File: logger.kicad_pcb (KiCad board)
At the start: 4 copper layers, 50.8 x 25.4 mm, 82 parts, among them IC1 ATMEGA1284P-A, P1 CONN_5X2, P2 CONN_2, U1 LT1615-1, U10 SN74AUP1G00, U2 AT45DB321D, U3 MCP6054, U4 MAX11612, U5 TPS7703X, U6 ADXL337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

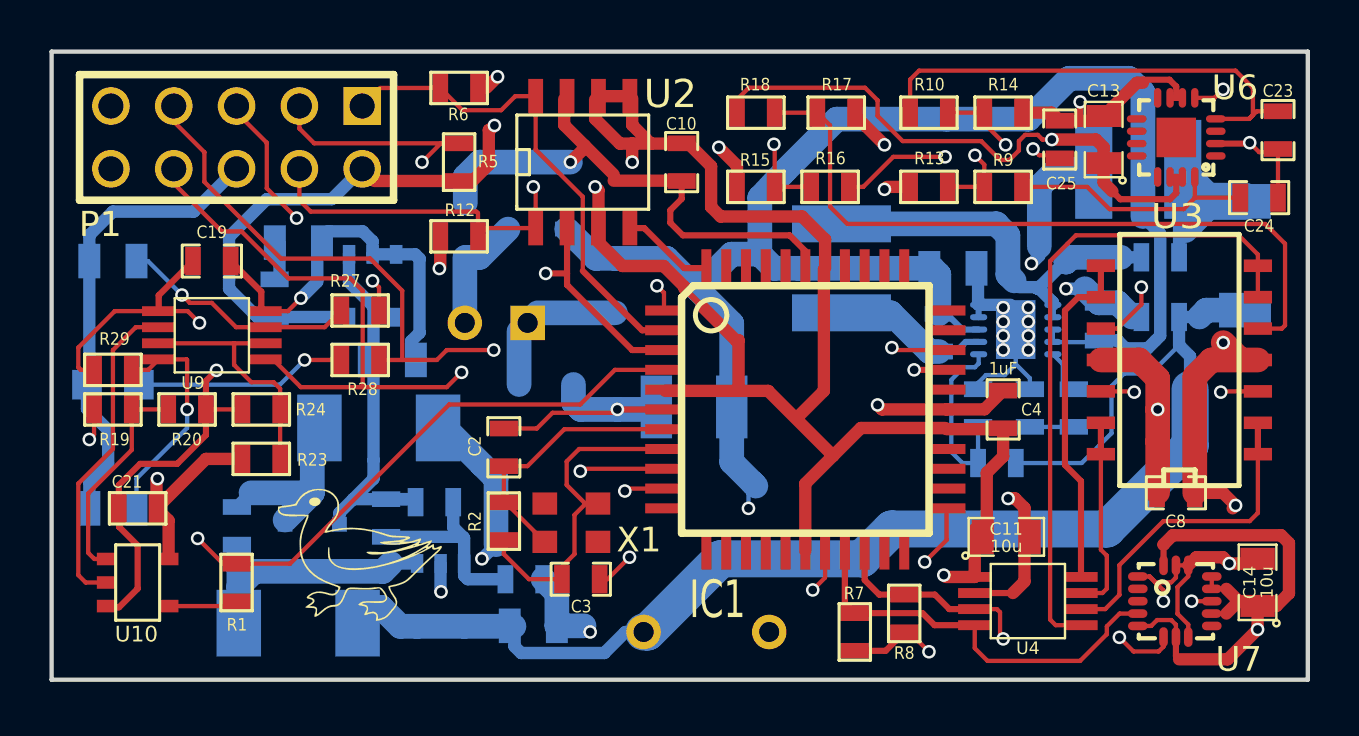
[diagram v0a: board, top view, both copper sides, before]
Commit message: General layout/grounding tweaks, DC-DC layout improved, ADC set up for Vdd as ref, switchable 3v3_Analog for lower standby power, reset circuitry redone, Footprint fixes, better silkscreen.
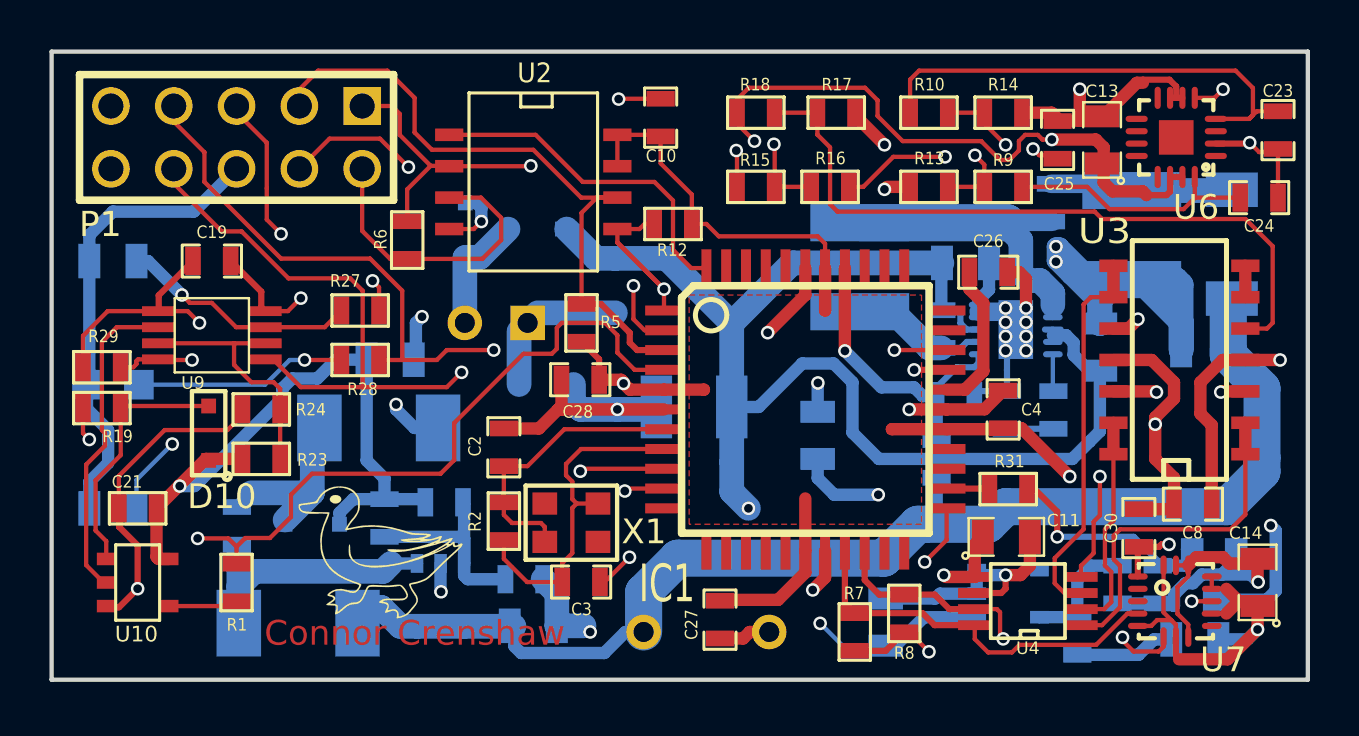
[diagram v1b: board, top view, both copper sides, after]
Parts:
- added C26: C, SM0603_Capa, F.Cu at (142.4, 100.5)
- added C27: 1u, SM0603_Capa, F.Cu at (131.6, 114.6)
- added C28: 1u, SM0603_Capa, F.Cu at (125.9, 104.9)
- added C29: 10u, SM0805, B.Cu at (138.2, 114.7)
- added C30: 1u, SM0603_Capa, F.Cu at (148.5, 110.9)
- added D10: DIODESCH, SOD323, F.Cu at (110.9, 107.1)
- added L5: 10u, SM0805, B.Cu at (135.5, 107.2)
- added Q1: MOS_P, SOT23GDS, B.Cu at (151.5, 112.8)
- added R30: 1, SM0603, B.Cu at (147.6, 113.2)
- added R31: 1k, SM0603, F.Cu at (143.2, 109.3)
- C18, C22: footprint SM0603_Capa -> SM0805
- C19: value .1 -> .1u
- D6: footprint DO128 -> SOD128
- R19: value 750k -> 100k
- R20: value 250k -> 1M; moved to B.Cu
- U2: value AT45DB321D -> SST25VF064C; footprint SO8E -> SST25_S3A
- U3: footprint SO14N -> SO14E
- U6: footprint LFCSP8 -> LFCSP16
- moved R20 39.9 mm to (149.3, 113.2), turned to 90 degrees
- moved C12 39.6 mm to (150.8, 115.4)
- moved R11 35.2 mm to (146.0, 115.3), turned to 270 degrees
- moved U5 28.6 mm to (143.2, 113.5), turned to 90 degrees
- moved R12 8.66 mm to (129.7, 98.6), turned to 0 degrees
- moved R5 8.17 mm to (126.0, 102.6)
- moved R6 6.50 mm to (118.9, 99.2), turned to 270 degrees
- moved C17 4.94 mm to (144.9, 97.7), turned to 90 degrees
- moved L4 2.67 mm to (148.2, 99.0), turned to 270 degrees
- moved R25 2.44 mm to (140.3, 108.1), turned to 90 degrees
- moved C18 2.24 mm to (151.2, 103.7)
- moved U2 2.15 mm to (124.0, 96.9), turned to 270 degrees
- moved C10 1.99 mm to (129.2, 94.3), turned to 90 degrees
- moved R26 1.03 mm to (141.1, 105.6), turned to 0 degrees
- moved C22 1.03 mm to (146.9, 103.6)
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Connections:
- C11 pad 1: 3V3 -> 3V3_Analog_Unswitched
- C13 pad 1: 3V3 -> 3V3_Analog
- C14 pad 2: 3V3 -> 3V3_Analog_Unswitched
- C7 pad 1: N-0000027 -> 3V3
- C8 pad 1: 3V3 -> 3V3_Analog
- C9 pad 1: N-0000027 -> 3V3
- D1 pad 2: N-0000027 -> 3V3
- IC1 pad 1: N-000009 -> Net-(IC1-Pad1)
- IC1 pad 11: N-0000046 -> (no net)
- IC1 pad 12: N-0000037 -> (no net)
- IC1 pad 13: N-0000033 -> (no net)
- IC1 pad 14: N-0000036 -> (no net)
- IC1 pad 15: N-0000039 -> (no net)
- IC1 pad 16: N-0000042 -> (no net)
- IC1 pad 2: N-0000012 -> Net-(IC1-Pad2)
- IC1 pad 21: N-0000047 -> (no net)
- IC1 pad 22: N-0000030 -> (no net)
- IC1 pad 25: N-0000040 -> (no net)
- IC1 pad 26: N-0000043 -> (no net)
- IC1 pad 3: N-0000050 -> Net-(IC1-Pad3)
- IC1 pad 32: N-0000031 -> (no net)
- IC1 pad 33: N-0000034 -> (no net)
- IC1 pad 34: N-0000038 -> (no net)
- IC1 pad 35: N-0000041 -> (no net)
- IC1 pad 36: N-0000044 -> (no net)
- IC1 pad 37: N-0000052 -> Vmon
- IC1 pad 40: N-0000045 -> (no net)
- IC1 pad 41: N-0000048 -> (no net)
- IC1 pad 42: N-0000032 -> (no net)
- IC1 pad 43: N-0000035 -> (no net)
- IC1 pad 44: N-000008 -> Net-(IC1-Pad44)
- P1 pad 1: N-0000012 -> Net-(IC1-Pad2)
- P1 pad 3: N-0000050 -> Net-(IC1-Pad3)
- P1 pad 4: N-000009 -> Net-(IC1-Pad1)
- R11 pad 1: 3V3 -> Net-(R11-Pad1)
- R12 pad 1: N-000009 -> Net-(IC1-Pad1)
- R18 pad 1: 3V3 -> 3V3_Analog
- R19 pad 2: VIN -> Net-(D10-Pad1)
- R20 pad 1: VIN -> 3V3_Analog_Unswitched
- R20 pad 2: GND -> Net-(Q1-PadG)
- R25 pad 2: N-0000066 -> Vmon
- R26 pad 1: N-0000066 -> Vmon
- R3 pad 1: N-0000027 -> 3V3
- R5 pad 1: N-0000050 -> Net-(IC1-Pad3)
- R6 pad 1: N-0000012 -> Net-(IC1-Pad2)
- R7 pad 2: 3V3 -> 3V3_Analog_Unswitched
- R8 pad 2: 3V3 -> 3V3_Analog_Unswitched
- U10 pad 1: VIN -> Net-(D10-Pad1)
- U2 pad 1: N-000009 -> Net-(IC1-Pad44)
- U2 pad 2: N-0000050 -> Net-(IC1-Pad2)
- U2 pad 4: N-000008 -> GND
- U2 pad 5: 3V3 -> Net-(IC1-Pad1)
- U2 pad 6: 3V3 -> Net-(IC1-Pad3)
- U2 pad 7: GND -> 3V3
- U2 pad 8: N-0000012 -> 3V3
- U3 pad 1: N-0000019 -> Net-(U3-Pad1)
- U3 pad 13: N-0000058 -> Net-(U3-Pad13)
- U3 pad 14: N-0000058 -> Net-(U3-Pad13)
- U3 pad 2: N-0000019 -> Net-(U3-Pad1)
- U3 pad 4: 3V3 -> 3V3_Analog
- U3 pad 6: N-0000057 -> Net-(U3-Pad6)
- U3 pad 7: N-0000057 -> Net-(U3-Pad6)
- U3 pad 8: N-0000018 -> Net-(U3-Pad8)
- U3 pad 9: N-0000018 -> Net-(U3-Pad8)
- U4 pad 1: N-0000057 -> Net-(U3-Pad1)
- U4 pad 2: N-0000019 -> Net-(U3-Pad13)
- U4 pad 3: N-0000058 -> Net-(U3-Pad8)
- U4 pad 4: N-0000018 -> 3V3_Analog
- U4 pad 5: 3V3 -> 3V3_Analog_Unswitched
- U5 pad 1: N-0000027 -> Net-(C29-Pad1)
- U5 pad 4: N-0000028 -> (no net)
- U5 pad 5: 3V3 -> Net-(R11-Pad1)
- U6 pad 14: 3V3 -> 3V3_Analog
- U6 pad 15: 3V3 -> 3V3_Analog
- U7 pad 14: 3V3 -> 3V3_Analog_Unswitched
- U7 pad 15: 3V3 -> 3V3_Analog_Unswitched
- U7 pad 8: 3V3 -> 3V3_Analog_Unswitched
- U7 pad 9: N-0000056 -> (no net)
- U8 pad 1: N-0000066 -> Vmon
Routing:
- net 3V3_Analog: track 0.00 -> 94.8 mm, vias 0 -> 5
- net 3V3: track 223.3 -> 131.7 mm, vias 15 -> 7
- net 3V3_Analog_Unswitched: track 0.00 -> 40.9 mm, vias 0 -> 3
- net Net-(IC1-Pad1): track 0.00 -> 29.8 mm, vias 0 -> 2
- net N-0000057: track 26.7 -> 0.00 mm
- net Net-(IC1-Pad3): track 0.00 -> 26.5 mm
- net N-0000050: track 25.8 -> 0.00 mm, vias 2 -> 0
- net N-000009: track 21.6 -> 0.00 mm, vias 2 -> 0
- net Net-(IC1-Pad2): track 0.00 -> 20.3 mm, vias 0 -> 2
- net N-0000012: track 20.1 -> 0.00 mm
- net Net-(C29-Pad1): track 0.00 -> 16.9 mm, vias 0 -> 2
- net Net-(U3-Pad8): track 0.00 -> 15.6 mm
- net N-0000027: track 15.5 -> 0.00 mm
- net Net-(U3-Pad1): track 0.00 -> 14.3 mm
- net N-0000018: track 14.0 -> 0.00 mm
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- added copper zone on F.Cu, net 3V3
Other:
- rule trace_min: 0.175 -> 0.00689
- rule via_min_size: 0.013 -> 0.000512
- board text added: "CC-BY-SA 3.0"
- board text added: "Connor Crenshaw"
- board text added: "OSHW"
- board text added: "Rev. 0"
- board text removed: "CC-BY-SA 3.0 OSHW"
- board text removed: "Rev. 02"
